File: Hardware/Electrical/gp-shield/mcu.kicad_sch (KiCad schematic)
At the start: 67 parts, among them J3 Conn_01x04, SW2 SW_Push, SW3 SW_Push

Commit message: Added net classes
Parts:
- F10, F11, F12, F13, F14, F15, F16, F17, F18, F19, F2, F20, F21, F22, F3, F4, F5, F6, F7, F8, F9: footprint Fuse:Fuse_0603_1608Metric_Pad1.05x0.95mm_HandSolder -> Fuse:Fuse_0805_2012Metric_Pad1.15x1.40mm_HandSolder
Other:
- note added: "PCINT gruoups are 0-7, 8-14, 16-23 PCINT0 and PCINT1 are used by moor sheld, so should leave general urpose pcint pins on pcint2 rthat is pd[0..7]"
- note added: "have n channel fet on led output?"
- note added: "use pd2, pd4 or pd7 pd2 can be pwm (oc3b or oc4b) so use for led then pd4 or pd7 for pb."
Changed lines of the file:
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@@
     (stroke (width 0) (type default) (color 0 0 0 0))
+  )
+  (text "use pd2, pd4 or pd7\npd2 can be pwm (oc3b or oc4b) so use for led\nthen pd4 or pd7 for pb.\n"
+    (at 63.5 58.42 0)
+    (effects (font (size 1.27 1.27)) (justify left bottom))
+  )
+  (text "PCINT gruoups are 0-7, 8-14, 16-23\n\nPCINT0 and PCINT1 are used by moor sheld, so should leave general urpose pcint pins on pcint2\n\nrthat is pd[0..7]"
+    (at 135.89 58.42 0)
+    (effects (font (size 1.27 1.27)) (justify left bottom))
   )
   (text "States:\n- Vbatt connected and USB connected.\n	- need reverse current protection on 5V reg, or some current limiting\n- Vbatt connected and no USB\n	- arduino 5V needs to be powered from shield\n- arduino vin connected and no Vbatt\n	- shield can be powered off arduino but shouldnt reverse current through regs.\n- \n- "
@@
   (text "Is protection needed on all digital pins as well?\nAnd do we need a ribbon style connector for port D and port B?"
     (at 212.09 48.26 0)
+    (effects (font (size 1.27 1.27)) (justify left bottom))
+  )
+  (text "have n channel fet on led output?" (at 63.5 66.04 0)
     (effects (font (size 1.27 1.27)) (justify left bottom))
   )
@@
       (effects (font (size 1.27 1.27)) hide)
     )
-    (property "Footprint" "Fuse:Fuse_0603_1608Metric_Pad1.05x0.95mm_HandSolder" (id 2) (at 66.04 92.71 0)
+    (property "Footprint" "Fuse:Fuse_0805_2012Metric_Pad1.15x1.40mm_HandSolder" (id 2) (at 66.04 92.71 0)
       (effects (font (size 1.27 1.27)) (justify left) hide)
     )
@@
       (effects (font (size 1.27 1.27)) hide)
     )
-    (property "Footprint" "Fuse:Fuse_0603_1608Metric_Pad1.05x0.95mm_HandSolder" (id 2) (at 66.04 105.41 0)
+    (property "Footprint" "Fuse:Fuse_0805_2012Metric_Pad1.15x1.40mm_HandSolder" (id 2) (at 66.04 105.41 0)
       (effects (font (size 1.27 1.27)) (justify left) hide)
     )
@@
       (effects (font (size 1.27 1.27)) hide)
     )
-    (property "Footprint" "Fuse:Fuse_0603_1608Metric_Pad1.05x0.95mm_HandSolder" (id 2) (at 234.95 115.57 0)
+    (property "Footprint" "Fuse:Fuse_0805_2012Metric_Pad1.15x1.40mm_HandSolder" (id 2) (at 234.95 115.57 0)
       (effects (font (size 1.27 1.27)) (justify left) hide)
     )
@@
       (effects (font (size 1.27 1.27)) hide)
     )
-    (property "Footprint" "Fuse:Fuse_0603_1608Metric_Pad1.05x0.95mm_HandSolder" (id 2) (at 234.95 113.03 0)
+    (property "Footprint" "Fuse:Fuse_0805_2012Metric_Pad1.15x1.40mm_HandSolder" (id 2) (at 234.95 113.03 0)
       (effects (font (size 1.27 1.27)) (justify left) hide)
     )
@@
       (effects (font (size 1.27 1.27)) hide)
     )
-    (property "Footprint" "Fuse:Fuse_0603_1608Metric_Pad1.05x0.95mm_HandSolder" (id 2) (at 81.28 148.59 0)
+    (property "Footprint" "Fuse:Fuse_0805_2012Metric_Pad1.15x1.40mm_HandSolder" (id 2) (at 81.28 148.59 0)
       (effects (font (size 1.27 1.27)) (justify left) hide)
     )
@@
       (effects (font (size 1.27 1.27)) hide)
     )
-    (property "Footprint" "Fuse:Fuse_0603_1608Metric_Pad1.05x0.95mm_HandSolder" (id 2) (at 81.28 153.67 0)
+    (property "Footprint" "Fuse:Fuse_0805_2012Metric_Pad1.15x1.40mm_HandSolder" (id 2) (at 81.28 153.67 0)
       (effects (font (size 1.27 1.27)) (justify left) hide)
     )
@@
       (effects (font (size 1.27 1.27)) hide)
     )
-    (property "Footprint" "Fuse:Fuse_0603_1608Metric_Pad1.05x0.95mm_HandSolder" (id 2) (at 234.95 102.87 0)
+    (property "Footprint" "Fuse:Fuse_0805_2012Metric_Pad1.15x1.40mm_HandSolder" (id 2) (at 234.95 102.87 0)
       (effects (font (size 1.27 1.27)) (justify left) hide)
     )
@@
       (effects (font (size 1.27 1.27)) hide)
     )
-    (property "Footprint" "Fuse:Fuse_0603_1608Metric_Pad1.05x0.95mm_HandSolder" (id 2) (at 234.95 100.33 0)
+    (property "Footprint" "Fuse:Fuse_0805_2012Metric_Pad1.15x1.40mm_HandSolder" (id 2) (at 234.95 100.33 0)
       (effects (font (size 1.27 1.27)) (justify left) hide)
     )
@@
       (effects (font (size 1.27 1.27)) hide)
     )
-    (property "Footprint" "Fuse:Fuse_0603_1608Metric_Pad1.05x0.95mm_HandSolder" (id 2) (at 234.95 107.95 0)
+    (property "Footprint" "Fuse:Fuse_0805_2012Metric_Pad1.15x1.40mm_HandSolder" (id 2) (at 234.95 107.95 0)
       (effects (font (size 1.27 1.27)) (justify left) hide)
     )
@@
       (effects (font (size 1.27 1.27)) hide)
     )
-    (property "Footprint" "Fuse:Fuse_0603_1608Metric_Pad1.05x0.95mm_HandSolder" (id 2) (at 66.04 100.33 0)
+    (property "Footprint" "Fuse:Fuse_0805_2012Metric_Pad1.15x1.40mm_HandSolder" (id 2) (at 66.04 100.33 0)
       (effects (font (size 1.27 1.27)) (justify left) hide)
     )
@@
       (effects (font (size 1.27 1.27)) hide)
     )
-    (property "Footprint" "Fuse:Fuse_0603_1608Metric_Pad1.05x0.95mm_HandSolder" (id 2) (at 66.04 90.17 0)
+    (property "Footprint" "Fuse:Fuse_0805_2012Metric_Pad1.15x1.40mm_HandSolder" (id 2) (at 66.04 90.17 0)
       (effects (font (size 1.27 1.27)) (justify left) hide)
     )
@@
       (effects (font (size 1.27 1.27)) hide)
     )
-    (property "Footprint" "Fuse:Fuse_0603_1608Metric_Pad1.05x0.95mm_HandSolder" (id 2) (at 234.95 110.49 0)
+    (property "Footprint" "Fuse:Fuse_0805_2012Metric_Pad1.15x1.40mm_HandSolder" (id 2) (at 234.95 110.49 0)
       (effects (font (size 1.27 1.27)) (justify left) hide)
     )
@@
       (effects (font (size 1.27 1.27)) hide)
     )
-    (property "Footprint" "Fuse:Fuse_0603_1608Metric_Pad1.05x0.95mm_HandSolder" (id 2) (at 66.04 102.87 0)
+    (property "Footprint" "Fuse:Fuse_0805_2012Metric_Pad1.15x1.40mm_HandSolder" (id 2) (at 66.04 102.87 0)
       (effects (font (size 1.27 1.27)) (justify left) hide)
     )
@@
       (effects (font (size 1.27 1.27)) hide)
     )
-    (property "Footprint" "Fuse:Fuse_0603_1608Metric_Pad1.05x0.95mm_HandSolder" (id 2) (at 81.28 146.05 0)
+    (property "Footprint" "Fuse:Fuse_0805_2012Metric_Pad1.15x1.40mm_HandSolder" (id 2) (at 81.28 146.05 0)
       (effects (font (size 1.27 1.27)) (justify left) hide)
     )
@@
       (effects (font (size 1.27 1.27)) hide)
     )
-    (property "Footprint" "Fuse:Fuse_0603_1608Metric_Pad1.05x0.95mm_HandSolder" (id 2) (at 81.28 151.13 0)
+    (property "Footprint" "Fuse:Fuse_0805_2012Metric_Pad1.15x1.40mm_HandSolder" (id 2) (at 81.28 151.13 0)
       (effects (font (size 1.27 1.27)) (justify left) hide)
     )
@@
       (effects (font (size 1.27 1.27)) hide)
     )
-    (property "Footprint" "Fuse:Fuse_0603_1608Metric_Pad1.05x0.95mm_HandSolder" (id 2) (at 81.28 156.21 0)
+    (property "Footprint" "Fuse:Fuse_0805_2012Metric_Pad1.15x1.40mm_HandSolder" (id 2) (at 81.28 156.21 0)
       (effects (font (size 1.27 1.27)) (justify left) hide)
     )
@@
       (effects (font (size 1.27 1.27)) hide)
     )
-    (property "Footprint" "Fuse:Fuse_0603_1608Metric_Pad1.05x0.95mm_HandSolder" (id 2) (at 66.04 97.79 0)
+    (property "Footprint" "Fuse:Fuse_0805_2012Metric_Pad1.15x1.40mm_HandSolder" (id 2) (at 66.04 97.79 0)
       (effects (font (size 1.27 1.27)) (justify left) hide)
     )
@@
       (effects (font (size 1.27 1.27)) hide)
     )
-    (property "Footprint" "Fuse:Fuse_0603_1608Metric_Pad1.05x0.95mm_HandSolder" (id 2) (at 66.04 95.25 0)
+    (property "Footprint" "Fuse:Fuse_0805_2012Metric_Pad1.15x1.40mm_HandSolder" (id 2) (at 66.04 95.25 0)
       (effects (font (size 1.27 1.27)) (justify left) hide)
     )
@@
       (effects (font (size 1.27 1.27)) hide)
     )
-    (property "Footprint" "Fuse:Fuse_0603_1608Metric_Pad1.05x0.95mm_HandSolder" (id 2) (at 81.28 158.75 0)
+    (property "Footprint" "Fuse:Fuse_0805_2012Metric_Pad1.15x1.40mm_HandSolder" (id 2) (at 81.28 158.75 0)
       (effects (font (size 1.27 1.27)) (justify left) hide)
     )
@@
       (effects (font (size 1.27 1.27)) hide)
     )
-    (property "Footprint" "Fuse:Fuse_0603_1608Metric_Pad1.05x0.95mm_HandSolder" (id 2) (at 66.04 87.63 0)
+    (property "Footprint" "Fuse:Fuse_0805_2012Metric_Pad1.15x1.40mm_HandSolder" (id 2) (at 66.04 87.63 0)
       (effects (font (size 1.27 1.27)) (justify left) hide)
     )
@@
       (effects (font (size 1.27 1.27)) hide)
     )
-    (property "Footprint" "Fuse:Fuse_0603_1608Metric_Pad1.05x0.95mm_HandSolder" (id 2) (at 234.95 105.41 0)
-      (effects (font (size 1.27 1.27)) (justify left) hide)
-    )
+    (property "Footprint" "Fuse:Fuse_0805_2012Metric_Pad1.15x1.40mm_HandSolder" (id 2) (at 234.95 105.41 0)
+      (effects (font (size 1.27 1.27)) (justify left) hide)
+    )

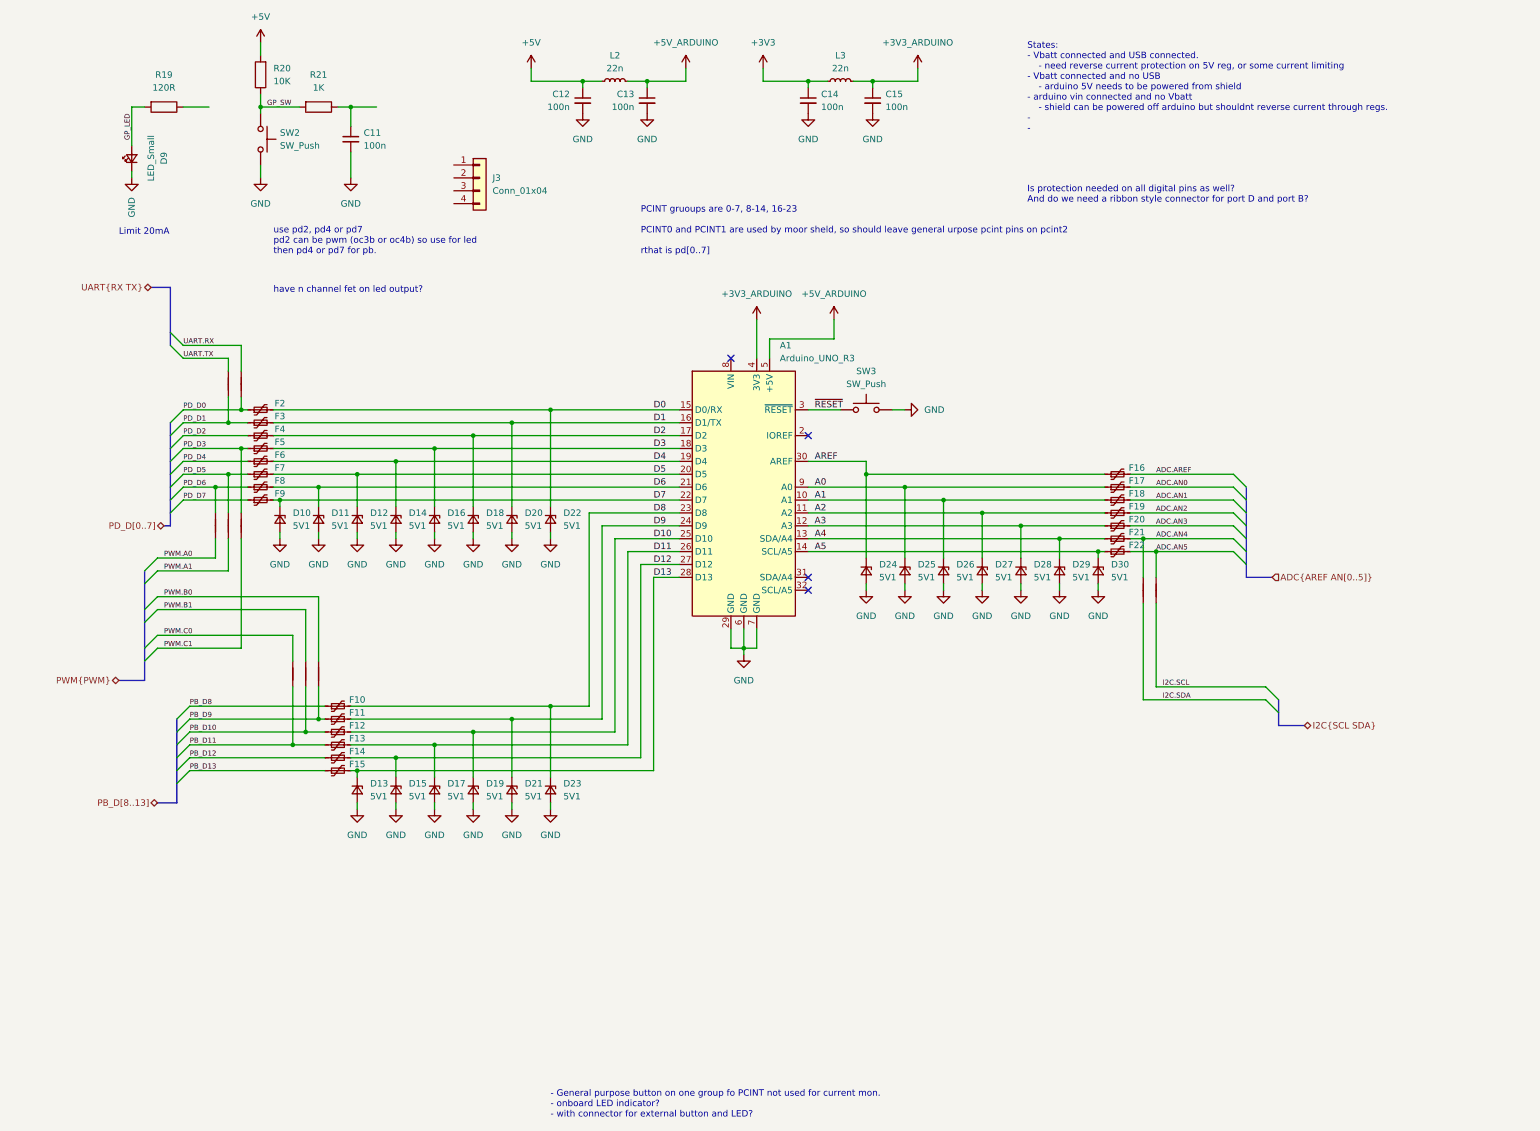
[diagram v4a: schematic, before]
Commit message: Added clamping diodes
Replaced zener regulator protection for GPIO with bidierectional schottky clamping diodes
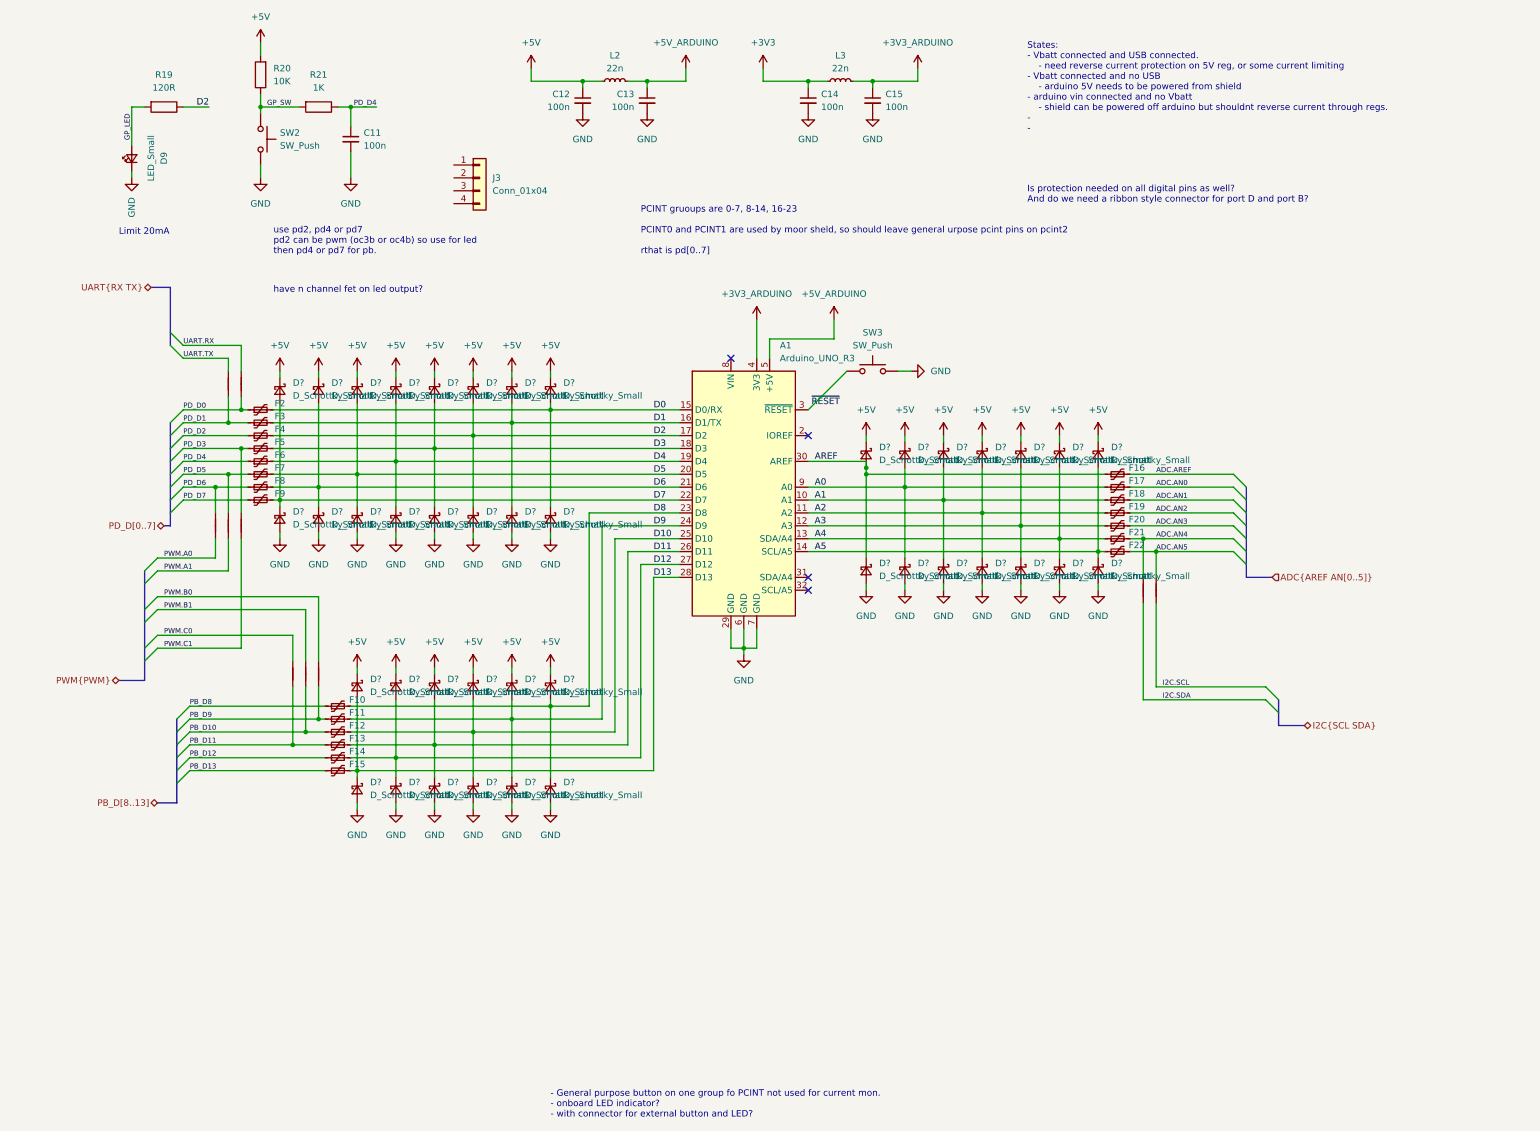
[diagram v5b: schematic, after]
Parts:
- removed D10, D11, D12, D13, D14, D15, D16, D17, D18, D19, D20, D21, D22, D23, D24, D25, D26, D27, D28, D29, D30: 5V1, Diode_SMD:D_0805_2012Metric_Pad1.15x1.40mm_HandSolder, symbol Device:D_Zener_Small
- added D? (x42): D_Schottky_Small, symbol Device:D_Schottky_Small
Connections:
- net +5V: now also D?.1 (K), D?.1 (K), D?.1 (K), D?.1 (K), D?.1 (K), D?.1 (K), D?.1 (K), D?.1 (K), D?.1 (K), D?.1 (K), D?.1 (K), D?.1 (K), D?.1 (K), D?.1 (K), D?.1 (K), D?.1 (K), D?.1 (K), D?.1 (K), D?.1 (K), D?.1 (K), D?.1 (K)
- net A0: now also D?.1 (K), D?.2 (A)
- net A1: now also D?.1 (K), D?.2 (A)
- net A2: now also D?.1 (K), D?.2 (A)
- net A3: now also D?.1 (K), D?.2 (A)
- net A4: now also D?.1 (K), D?.2 (A)
- net A5: now also D?.1 (K), D?.2 (A)
- net AREF: now also D?.1 (K), D?.2 (A)
- net D0: now also D?.1 (K), D?.2 (A)
- net D1: now also D?.1 (K), D?.2 (A)
- net D10: now also D?.1 (K), D?.2 (A)
- net D11: now also D?.1 (K), D?.2 (A)
- net D12: now also D?.1 (K), D?.2 (A)
- net D13: now also D?.1 (K), D?.2 (A)
- net D2: now also R19.1, D?.1 (K), D?.2 (A)
- net D3: now also D?.1 (K), D?.2 (A)
- net D4: now also D?.1 (K), D?.2 (A)
- net D5: now also D?.1 (K), D?.2 (A)
- net D6: now also D?.1 (K), D?.2 (A)
- net D7: now also D?.1 (K), D?.2 (A)
- net D8: now also D?.1 (K), D?.2 (A)
- net D9: now also D?.1 (K), D?.2 (A)
- net GND: now also D?.2 (A), D?.2 (A), D?.2 (A), D?.2 (A), D?.2 (A), D?.2 (A), D?.2 (A), D?.2 (A), D?.2 (A), D?.2 (A), D?.2 (A), D?.2 (A), D?.2 (A), D?.2 (A), D?.2 (A), D?.2 (A), D?.2 (A), D?.2 (A), D?.2 (A), D?.2 (A), D?.2 (A)
- net PD_D4: now also C11.1, R21.1
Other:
- moved on the sheet: SW3

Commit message: Major revisions
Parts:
- removed C14, C15: 100n, Capacitor_SMD:C_0805_2012Metric_Pad1.18x1.45mm_HandSolder, symbol Device:C_Small
- removed D? (x39): D_Schottky_Small, symbol Device:D_Schottky_Small
- removed L3: 22n, Inductor_SMD:L_0805_2012Metric_Pad1.15x1.40mm_HandSolder, symbol Device:L_Small
- added D11, D13, D14, D15, D16, D17, D18, D19, D20, D21, D22, D23, D24, D25, D26, D27, D28, D29, D30, D31, D32, D33, D34, D35, D36, D37, D38, D39, D40, D41, D42, D43, D44, D45, D46, D47, D48, D49, D9: D_Schottky_Small, Diode_SMD:D_0805_2012Metric_Pad1.15x1.40mm_HandSolder, symbol Device:D_Schottky_Small
- added JP1: Jumper_2_Open, Connector_PinHeader_2.54mm:PinHeader_1x02_P2.54mm_Vertical, symbol Jumper:Jumper_2_Open
- added Q3: Q_NMOS_GDS, Package_TO_SOT_SMD:SOT-23, symbol Device:Q_NMOS_GDS
- D10, D12, D8: renamed from D?; footprint (none) -> Diode_SMD:D_0805_2012Metric_Pad1.15x1.40mm_HandSolder
- renumbered C13 to C10, C11 to C8, C12 to C9, D9 to D7, F9 to F10, F10 to F11, F11 to F12, F12 to F13, F13 to F14, F14 to F15, F15 to F16, F16 to F17, F17 to F18, F18 to F19, F19 to F20, F20 to F21, F21 to F22, F22 to F23, F2 to F3, F3 to F4, F4 to F5, F5 to F6, F6 to F7, F7 to F8, F8 to F9, R19 to R16, R20 to R17, R21 to R18
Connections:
- net +5V: now also J3.1 (Pin_1), R16.1, D14.1 (K), D16.1 (K), D18.1 (K), D20.1 (K), D22.1 (K), D24.1 (K), D26.1 (K), D28.1 (K), D30.1 (K), D32.1 (K), D34.1 (K), D36.1 (K), D38.1 (K), D40.1 (K), D42.1 (K), D44.1 (K), D46.1 (K), D48.1 (K), JP1.1 (A); no longer C9.1, L2.2
- net A0: now also D38.2 (A), D39.1 (K)
- net A1: now also D40.2 (A), D41.1 (K)
- net A2: now also D42.2 (A), D43.1 (K)
- net A3: now also D44.2 (A), D45.1 (K)
- net A4: now also D46.2 (A), D47.1 (K)
- net A5: now also D48.2 (A), D49.1 (K)
- net AREF: now also D36.2 (A), D37.1 (K)
- net D0: now also D32.2 (A), D33.1 (K)
- net D1: now also D28.2 (A), D29.1 (K)
- net D10: now also D26.2 (A), D27.1 (K)
- net D11: now also D22.2 (A), D23.1 (K)
- net D12: now also D18.2 (A), D19.1 (K)
- net D13: now also D14.2 (A), D15.1 (K)
- net D2: now also D24.2 (A), D25.1 (K); no longer R16.1
- net D3: now also D20.2 (A), D21.1 (K)
- net D4: now also D16.2 (A), D17.1 (K)
- net D5: now also D13.1 (K)
- net D6: now also D11.1 (K)
- net D7: now also D9.1 (K)
- net D8: now also D34.2 (A), D35.1 (K)
- net D9: now also D30.2 (A), D31.1 (K)
- net GND: now also J3.4 (Pin_4), D11.2 (A), D13.2 (A), D15.2 (A), D17.2 (A), D19.2 (A), D21.2 (A), D23.2 (A), D25.2 (A), D27.2 (A), D29.2 (A), D31.2 (A), D33.2 (A), D35.2 (A), D37.2 (A), D39.2 (A), D41.2 (A), D43.2 (A), D45.2 (A), D47.2 (A), D49.2 (A), D9.2 (A), Q3.2 (D); no longer D7.1 (K)
- net PD_D2: now also Q3.1 (G)
- net PD_D4: now also J3.3 (Pin_3)
- net LED_OUT: now reaches J3.2 (Pin_2)
- net LED_OUT: now also D7.1 (K), Q3.3 (S)
- new net +5V_JMP: C9.1, JP1.2 (B), L2.2
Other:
- note removed: "have n channel fet on led output?"
- moved on the sheet: C10, C8, C9, D7, F10, F11, F12, F13, F14, F15, F16, F17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

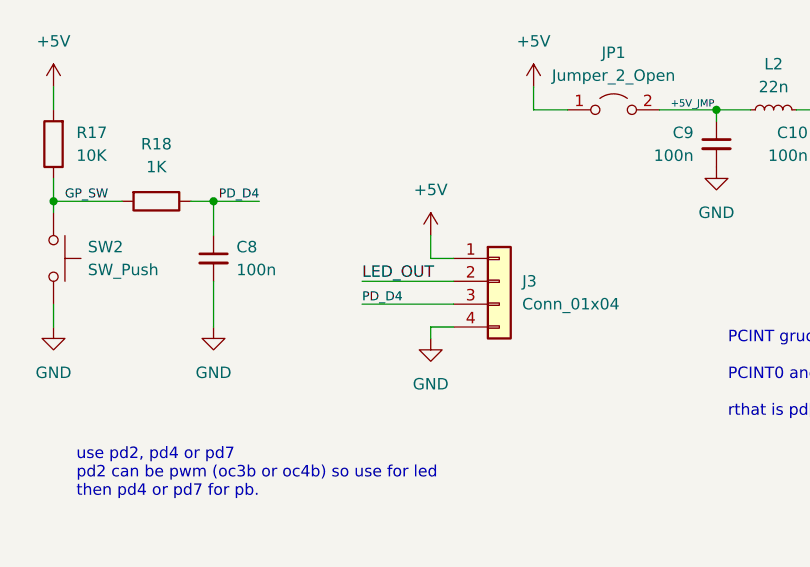
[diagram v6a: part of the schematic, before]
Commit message: Major PCB changes
Added combined footprint for XT60 and terminal port.
Fixed polarity of Batt and PWR_out connectors.
Standardised polarity markers to show negative on white.
Moved Port D and Port B connectors to be inline with existing arduino connectors. Removed extra pins.
Added analogue in-line output.
Adjusted component placement for more space around power supply and GP PB and LED.
Draft version of track routing - incomplete.
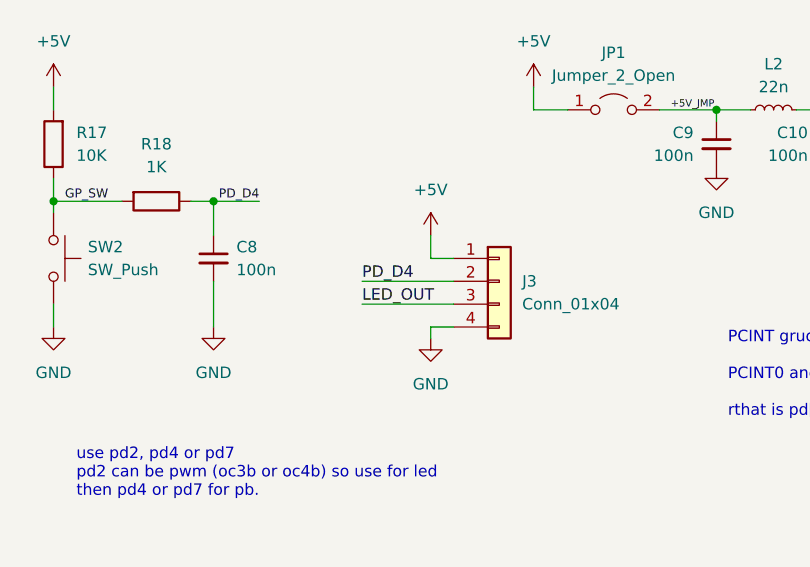
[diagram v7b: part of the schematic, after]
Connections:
- net LED_OUT: now also J3.3 (Pin_3); no longer J3.2 (Pin_2)
- net PD_D4: now also J3.2 (Pin_2); no longer J3.3 (Pin_3)
